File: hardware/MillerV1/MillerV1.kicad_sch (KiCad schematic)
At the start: 298 parts, among them Q1 Q12MHz/20pF/10ppm/4P/3.2x2.5mm, U1 CCGM1A1(FBGA-324), U10 RP2040(QFN-56_7x7mm_P0.4mm), U11 TPS62A02ADRLR(SOT-563-6), U12 TPS62A02ADRLR(SOT-563-6), U13 TPS62A02ADRLR(SOT-563-6), U14 TPS62A02ADRLR(SOT-563-6), U15 TPS62A02ADRLR(SOT-563-6), U2 HX7027(SOT-23-3), U3 NA(ZD25WQ16CSIGT(SOIC-8_208mi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, U4 NA(MCP120T-300I/TT(SOT-23-3)), U5 TXB0108PWR(TSSOP-20), U6 TXB0108PWR(TSSOP-20), U7 LY68S3200SLT(SOIC-8_150mil), U8 ZD25WQ16CSIGT(SOIC-8_208mils), U9 LY68S3200SLT(SOIC-8_150mil)

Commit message: updated
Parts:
- MH1, MH2, MH3, MH4: footprint OLIMEX_Other-FP:Mounting_Hole_Drill-3.3mm_Clerance-7mm -> MountingHole:MountingHole_3.2mm_M3_Pad_Via
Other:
- moved on the sheet: C100, C88, C95, FET1, FET2, PS2_KBD1, R23, R24, R29, R30, R32, R33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

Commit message: made room for tobi
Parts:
- removed C88: 100nF/10V/20%/X5R/C0402, OLIMEX_RLC-FP:C_0402_5MIL_DWS, symbol OLIMEX_RCL:C
- removed FET1, FET2: BSS138(SOT-23-3), OLIMEX_Transistors-FP:SOT23, symbol OLIMEX_Transistors:N-MOS+DIOD
- removed PS2_KBD1: MDR6_MINI-DIN, OLIMEX_Connectors-FP:PS2_MDR6_MINI-DIN, symbol OLIMEX_Connectors:PS2_MDR6_MINI-DIN
- removed R23, R24, R29, R30: 10k/R0402, OLIMEX_RLC-FP:R_0402_5MIL_DWS, symbol OLIMEX_RCL:R
- removed R32, R37, R41: 430R/1%/R0402, OLIMEX_RLC-FP:R_0402_5MIL_DWS, symbol OLIMEX_RCL:R
- removed R33, R38, R42: 866R/1%/R0402, OLIMEX_RLC-FP:R_0402_5MIL_DWS, symbol OLIMEX_RCL:R
- removed R34, R39, R43: 2.05k/1%/R0402, OLIMEX_RLC-FP:R_0402_5MIL_DWS, symbol OLIMEX_RCL:R
- removed R35, R40, R44: 4.42k/1%/R0402, OLIMEX_RLC-FP:R_0402_5MIL_DWS, symbol OLIMEX_RCL:R
- removed TVS1, TVS2, TVS3, TVS4, TVS5: NA(GG0402052R542P), OLIMEX_Diodes-FP:D_0402_5MIL_DWS, symbol OLIMEX_Diodes:GG0402052R542P
- removed VGA1: HDR15-3.08-14.5T/VGA15/14.5mm, OLIMEX_Connectors-FP:VGA15-F(HDR15-3.08-14.5T)_DrillSlot, symbol OLIMEX_Connectors:VGA15-F(CD0515S21J0)
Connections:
- no-connect marks 8 -> 3
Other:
- note added: "ISO Interface"
- note added: "USB PHY"
- note removed: "PS/2 Port"
- note removed: "PS2_CLK_5V"
- note removed: "PS2_DATA_5V"
- note removed: "VGA"
- moved on the sheet: C100, C95, R53, R54, R57, R58, U7, U9

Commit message: made room for tobi
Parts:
- added IC1: TUSB1106PWR, New_Libary:SOP65P640X120-16N, symbol New_Library:TUSB1106PWR
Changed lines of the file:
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@@
+	)
+	(symbol
+		(lib_id "New_Library:TUSB1106PWR")
+		(at 612.14 119.38 0)
+		(unit 1)
+		(exclude_from_sim no)
+		(in_bom yes)
+		(on_board yes)
+		(dnp no)
+		(fields_autoplaced yes)
+		(property "Reference" "IC1"
+			(at 636.27 111.76 0)
+			(effects
+				(font
+					(size 1.27 1.27)
+				)
+			)
+		)
+		(property "Value" "TUSB1106PWR"
+			(at 636.27 114.3 0)
+			(effects
+				(font
+					(size 1.27 1.27)
+				)
+			)
+		)
+		(property "Footprint" "New_Libary:SOP65P640X120-16N"
+			(at 656.59 214.3 0)
+			(effects
+				(font
+					(size 1.27 1.27)
+				)
+				(justify left top)
+				(hide yes)
+			)
+		)
+		(property "Datasheet" "http://www.ti.com/lit/gpn/tusb1106"
+			(at 656.59 314.3 0)
+			(effects
+				(font
+					(size 1.27 1.27)
+				)
+				(justify left top)
+				(hide yes)
+			)
+		)
+		(property "Description" "Texas Instruments TUSB1106PWR, USB Transceiver, USB 2.0 at 12Mbit/s, 3.3 V, 5 V, 16-Pin TSSOP"
+			(at 612.14 119.38 0)
+			(effects
+				(font
+					(size 1.27 1.27)
+				)
+				(hide yes)
+			)
+		)
+		(property "Height" "1.2"
+			(at 656.59 514.3 0)
+			(effects
+				(font
+					(size 1.27 1.27)
+				)
+				(justify left top)
+				(hide yes)
+			)
+		)
+		(property "Mouser Part Number" "595-TUSB1106PWR"
+			(at 656.59 614.3 0)
+			(effects
+				(font
+					(size 1.27 1.27)
+				)
+				(justify left top)
+				(hide yes)
+			)
+		)
+		(property "Mouser Price/Stock" "https://www.mouser.co.uk/ProductDetail/Texas-Instruments/TUSB1106PWR?qs=7kv20MEVUlg2%2FxFfZrfm%2FA%3D%3D"
+			(at 656.59 714.3 0)
+			(effects
+				(font
+					(size 1.27 1.27)
+				)
+				(justify left top)
+				(hide yes)
+			)
+		)
+		(property "Manufacturer_Name" "Texas Instruments"
+			(at 656.59 814.3 0)
+			(effects
+				(font
+					(size 1.27 1.27)
+				)
+				(justify left top)
+				(hide yes)
+			)
+		)
+		(property "Manufacturer_Part_Number" "TUSB1106PWR"
+			(at 656.59 914.3 0)
+			(effects
+				(font
+					(size 1.27 1.27)
+				)
+				(justify left top)
+				(hide yes)
+			)
+		)
+		(property "Value 2M" ""
+			(at 612.14 119.38 0)
+			(effects
+				(font
+					(size 1.27 1.27)
+				)
+				(hide yes)
+			)
+		)
+		(pin "11"
+		)
+		(pin "8"
+		)
+		(pin "15"
+		)
+		(pin "13"
+		)
+		(pin "7"
+		)
+		(pin "16"
+		)
+		(pin "14"
+		)
+		(pin "10"
+		)
+		(pin "12"
+		)
+		(pin "9"
+		)
+		(pin "6"
+		)
+		(pin "5"
+		)
+		(pin "4"
+		)
+		(pin "3"
+		)
+		(pin "2"
+		)
+		(pin "1"
+		)
+		(instances
+			(project "MillerV1"
+				(path "/284a97db-b878-4d19-9282-298636eac808"
+					(reference "IC1")
+					(unit 1)
+				)
+			)
+		)
 	)
 	(symbol

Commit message: added VCC siwtcher for ISO Interface
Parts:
- removed Pmod1: F-R-2x06-LF, OLIMEX_Connectors-FP:Digilent_Pmod_12-pin, symbol OLIMEX_Connectors:Digilent_Pmod_12-pin
- added C127, C128: 22uF, Capacitor_SMD:C_0603_1608Metric_Pad1.08x0.95mm_HandSolder, symbol OLIMEX_RCL:C
- added J2: Conn_02x04_Counter_Clockwise, Connector_PinHeader_2.54mm:PinHeader_2x04_P2.54mm_Horizontal, symbol Connector_Generic:Conn_02x04_Counter_Clockwise
- added R23: 22k, Resistor_SMD:R_0402_1005Metric_Pad0.72x0.64mm_HandSolder, symbol Device:R_Small
- added R24: 50k, Resistor_SMD:R_0402_1005Metric_Pad0.72x0.64mm_HandSolder, symbol Device:R_Small
- added R29: 18.2k, Resistor_SMD:R_0402_1005Metric_Pad0.72x0.64mm_HandSolder, symbol Device:R_Small
- added U16: TLV75801PDBV, Package_TO_SOT_SMD:SOT-23-5, symbol Regulator_Linear:TLV75801PDBV
- added U18: SiP32432DR3, Package_TO_SOT_SMD:SOT-363_SC-70-6, symbol Power_Management:SiP32432DR3
- C10, C100, C101, C102, C103, C104, C105, C108, C109, C11, C12, C13, C14, C15, C16, C30, C42, C44, C46, C48, C59, C63, C67, C70, C75, C82, C85, C86, C87, C89, C9, C90, C91, C92, C94, C95, C96, C97, C98, C99: value 100nF/10V/20%/X5R/C0402 -> 100nF
- C112, C114, C118, C120, C124, C83: value 22uF/6.3V/20%/X5R/C0603 -> 22uF
- C113, C115, C119, C121, C125: value 47uF/6.3V/20%/X5R/C0805 -> 47uF
- C126, C39, C40: value 10uF/6.3V/X5R/20%/C0402 -> 10uF
- C84: value NA(100nF/10V/20%/X5R/C0402) -> NA(100nF)
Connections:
- net +2V5: now also U6.8 (A7), U6.9 (A8)
- net +3V3: no longer C90.1, U6.19 (Vccb)
- net +5V_USB: now also C128.1, U16.1 (IN), U18.4 (IN)
- net EA_A7: now also R29.2; no longer U6.8 (A7)
- net EA_B7: now also U16.3 (EN), U18.3 (~{ON}); no longer U6.9 (A8)
- net GND: now also C127.2, C128.2, J2.1 (Pin_1), R23.2, U16.2 (GND), U18.2 (GND), U18.5 (GND)
- net ISO_RST: now reaches U6.20 (B1)
- net ISO_RST: now also J2.3 (Pin_3)
- net ISO_IO: now reaches U6.17 (B3)
- net ISO_IO: now also J2.5 (Pin_5)
- net ISO_AS1: now reaches U6.15 (B5)
- net ISO_AS1: now also U6.14 (B6), J2.7 (Pin_7), J2.8 (Pin_8)
- net ISO_CLK: now reaches U6.18 (B2)
- net ISO_CLK: now also J2.4 (Pin_4)
- net ISO_AS0: now reaches U6.16 (B4)
- net ISO_AS0: now also J2.6 (Pin_6)
- new net FB_I: R23.1, R24.2, R29.1, U16.4 (FB)
- new net ISO: C127.1, C90.1, J2.2 (Pin_2), R24.1, U16.5 (OUT), U18.1 (OUT), U6.19 (Vccb)
- no-connect marks 3 -> 5
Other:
- note added: ".55V"
- note added: "ISO/IEC 7816 Interface"
- moved on the sheet: C90, C91, U6

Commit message: added VCC siwtcher for ISO Interface
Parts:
- added C88: 22uF, Capacitor_SMD:C_0603_1608Metric_Pad1.08x0.95mm_HandSolder, symbol OLIMEX_RCL:C
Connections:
- net GND: now also C88.2
- net ISO: now also C88.1
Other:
- moved on the sheet: C127, C128, C90, C91, FID1, FID10, FID11, FID12, FID2, FID3, FID4, FID5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

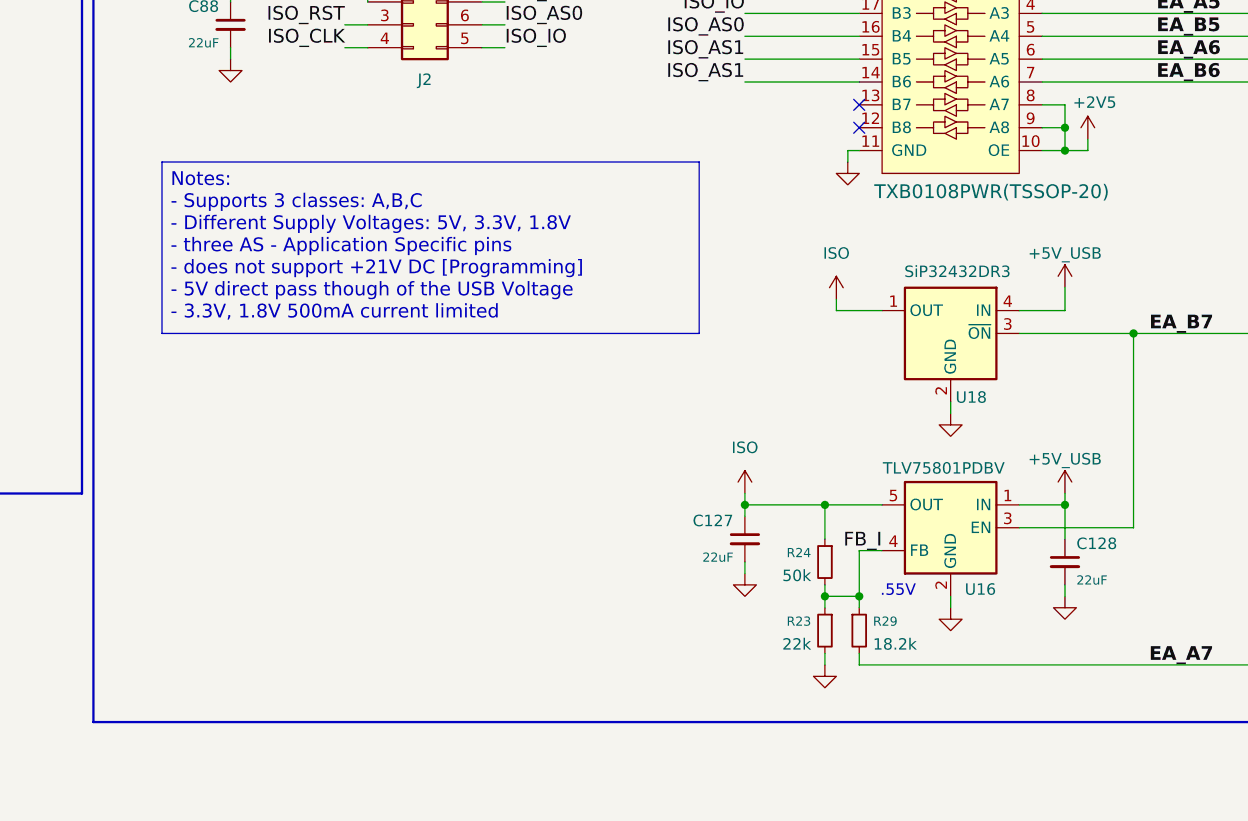
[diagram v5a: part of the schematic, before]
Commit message: added VCC siwtcher for ISO Interface
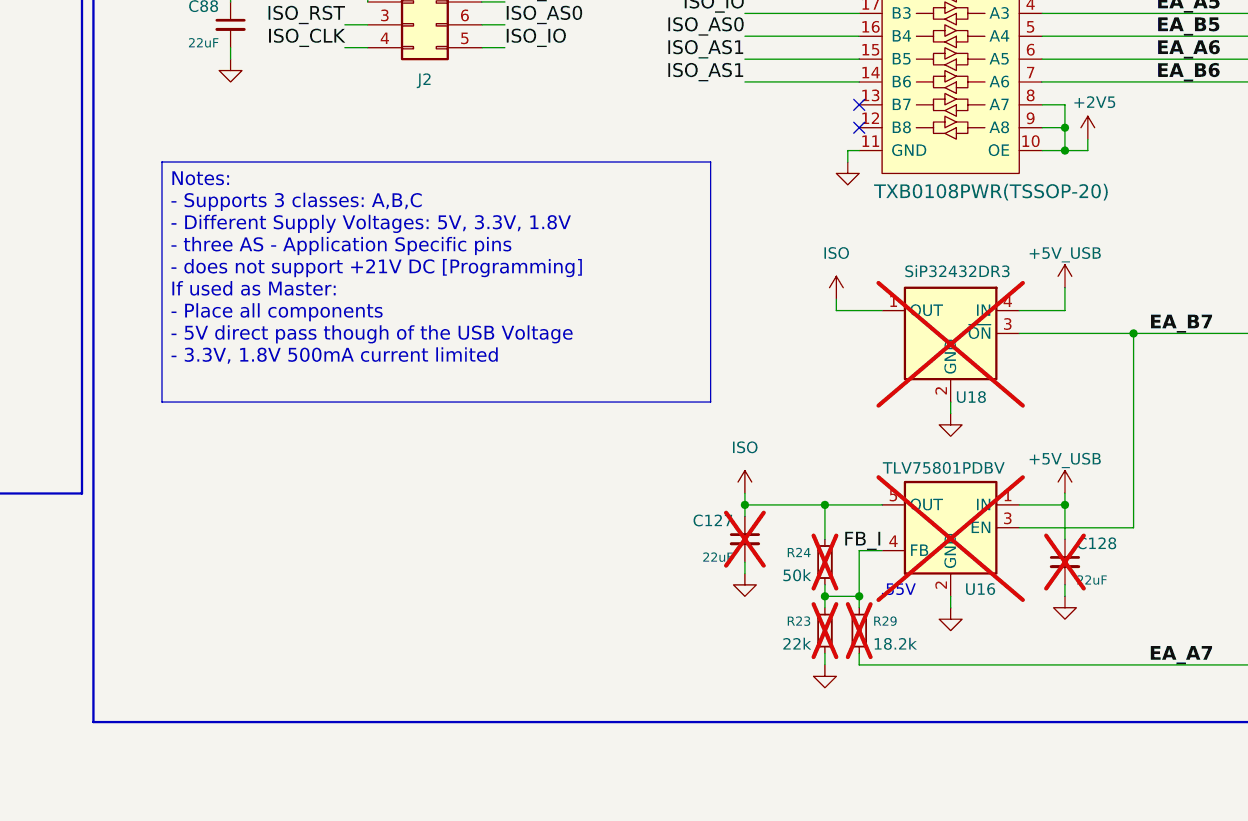
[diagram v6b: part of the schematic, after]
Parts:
- C127, C128, R23, R24, R29, U16, U18: now not fitted
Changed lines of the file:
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@@
 		)
 	)
-	(text_box "Notes:\n- Supports 3 classes: A,B,C\n- Different Supply Voltages: 5V, 3.3V, 1.8V\n- three AS - Application Specific pins\n- does not support +21V DC [Programming]\n- 5V direct pass though of the USB Voltage\n- 3.3V, 1.8V 500mA current limited"
+	(text_box "Notes:\n- Supports 3 classes: A,B,C\n- Different Supply Voltages: 5V, 3.3V, 1.8V\n- three AS - Application Specific pins\n- does not support +21V DC [Programming]\nIf used as Master:\n- Place all components\n- 5V direct pass though of the USB Voltage\n- 3.3V, 1.8V 500mA current limited"
 		(exclude_from_sim no)
 		(at 589.28 290.83 0)
-		(size 59.69 19.05)
+		(size 60.96 26.67)
 		(margins 0.9525 0.9525 0.9525 0.9525)
 		(stroke
@@
 			(table_cell "Vout"
 				(exclude_from_sim no)
-				(at 601.98 313.69 0)
+				(at 600.71 328.93 0)
 				(size 10.16 3.81)
 				(margins 0.9525 0.9525 0.9525 0.9525)
@@
 			(table_cell "EA_B7"
 				(exclude_from_sim no)
-				(at 612.14 313.69 0)
+				(at 610.87 328.93 0)
 				(size 8.89 3.81)
 				(margins 0.9525 0.9525 0.9525 0.9525)
@@
 			(table_cell "EA_A7"
 				(exclude_from_sim no)
-				(at 621.03 313.69 0)
+				(at 619.76 328.93 0)
 				(size 10.16 3.81)
 				(margins 0.9525 0.9525 0.9525 0.9525)
@@
 			(table_cell "5V"
 				(exclude_from_sim no)
-				(at 601.98 317.5 0)
+				(at 600.71 332.74 0)
 				(size 10.16 3.81)
 				(margins 0.9525 0.9525 0.9525 0.9525)
@@
 			(table_cell "LOW"
 				(exclude_from_sim no)
-				(at 612.14 317.5 0)
+				(at 610.87 332.74 0)
 				(size 8.89 3.81)
 				(margins 0.9525 0.9525 0.9525 0.9525)
@@
 			(table_cell "-"
 				(exclude_from_sim no)
-				(at 621.03 317.5 0)
+				(at 619.76 332.74 0)
 				(size 10.16 3.81)
 				(margins 0.9525 0.9525 0.9525 0.9525)
@@
 			(table_cell "3V3"
 				(exclude_from_sim no)
-				(at 601.98 321.31 0)
+				(at 600.71 336.55 0)
 				(size 10.16 3.81)
 				(margins 0.9525 0.9525 0.9525 0.9525)
@@
 			(table_cell "HIGH"
 				(exclude_from_sim no)
-				(at 612.14 321.31 0)
+				(at 610.87 336.55 0)
 				(size 8.89 3.81)
 				(margins 0.9525 0.9525 0.9525 0.9525)
@@
 			(table_cell "Z"
 				(exclude_from_sim no)
-				(at 621.03 321.31 0)
+				(at 619.76 336.55 0)
 				(size 10.16 3.81)
 				(margins 0.9525 0.9525 0.9525 0.9525)
@@
 			(table_cell "1V8"
 				(exclude_from_sim no)
-				(at 601.98 325.12 0)
+				(at 600.71 340.36 0)
 				(size 10.16 3.81)
 				(margins 0.9525 0.9525 0.9525 0.9525)
@@
 			(table_cell "HIGH"
 				(exclude_from_sim no)
-				(at 612.14 325.12 0)
+				(at 610.87 340.36 0)
 				(size 8.89 3.81)
 				(margins 0.9525 0.9525 0.9525 0.9525)
@@
 			(table_cell "LOW"
 				(exclude_from_sim no)
-				(at 621.03 325.12 0)
+				(at 619.76 340.36 0)
 				(size 10.16 3.81)
 				(margins 0.9525 0.9525 0.9525 0.9525)
@@
 		(in_bom yes)
 		(on_board yes)
-		(dnp no)
+		(dnp yes)
 		(property "Reference" "R24"
 			(at 661.416 334.264 0)
@@
 		(in_bom yes)
 		(on_board yes)
-		(dnp no)
+		(dnp yes)
 		(property "Reference" "U18"
 			(at 679.196 316.992 0)
@@
 		(in_bom yes)
 		(on_board yes)
-		(dnp no)
+		(dnp yes)
 		(property "Reference" "R23"
 			(at 661.416 341.884 0)
@@
 		(in_bom yes)
 		(on_board yes)
-		(dnp no)
+		(dnp yes)
 		(property "Reference" "C127"
 			(at 652.78 330.708 0)
@@
 		(in_bom yes)
 		(on_board yes)
-		(dnp no)
+		(dnp yes)
 		(property "Reference" "C128"
 			(at 690.88 333.248 0)
@@
 		(in_bom yes)
 		(on_board yes)
-		(dnp no)
+		(dnp yes)
 		(property "Reference" "U16"
 			(at 680.212 338.328 0)
@@
 		(in_bom yes)
 		(on_board yes)
-		(dnp no)
+		(dnp yes)
 		(property "Reference" "R29"
 			(at 668.274 341.884 0)
